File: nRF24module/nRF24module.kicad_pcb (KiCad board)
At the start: 2 copper layers, 40 x 20 mm, 31 parts, among them J1 SMA-RP, U1 nRF24L01P, U2 RFX2401C, X1 16MHz

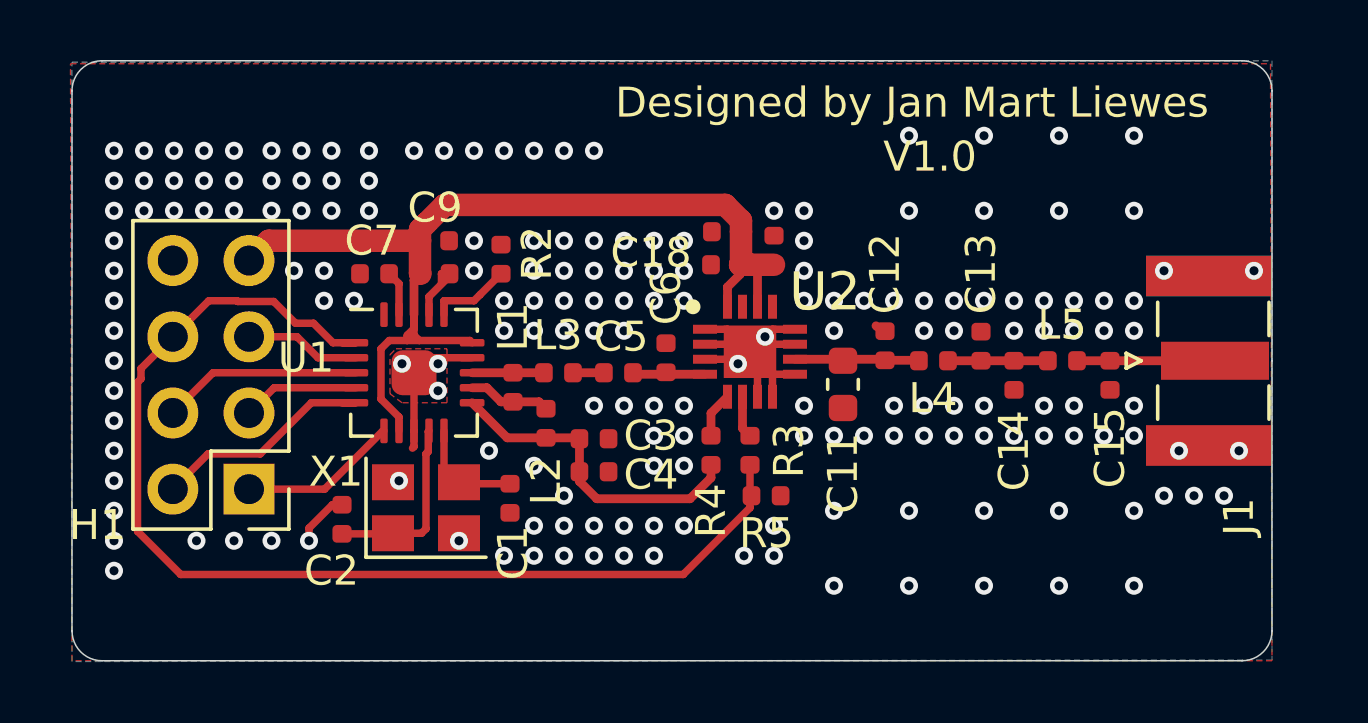
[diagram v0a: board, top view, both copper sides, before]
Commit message: Update, with Licence added to files, and rerouted PCB, cleaned up some things. Tightened up components, placed traces neater, placed vias neater. Added OSHW logo. TODO: Make own logo and add that.
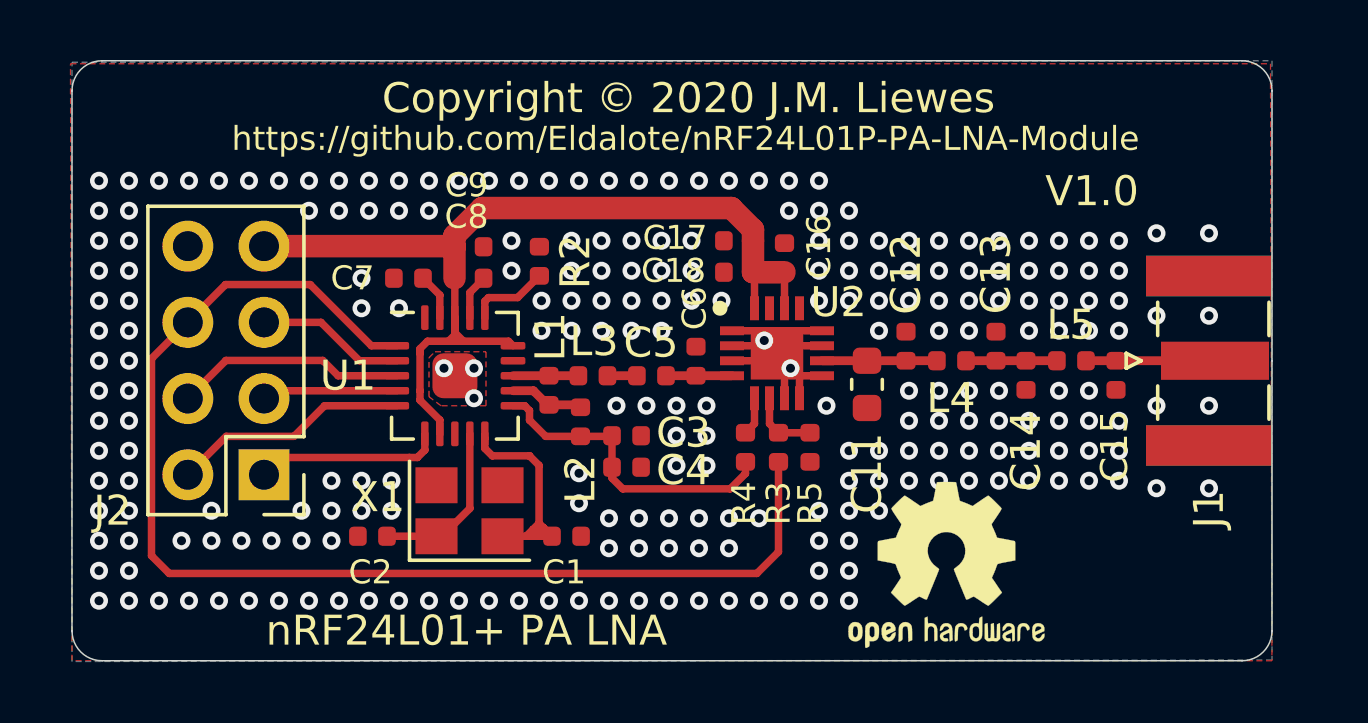
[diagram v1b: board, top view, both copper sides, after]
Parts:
- added LOGO1: Logo_Open_Hardware_Small, Symbol:OSHW-Logo2_7.3x6mm_SilkScreen, F.Cu at (148.8, 108.8)
- R5: value R_0402_1005Metric -> 2K
- moved C1 2.27 mm to (136.1, 107.8), turned to 180 degrees
- moved R5 2.18 mm to (144.2, 104.9), turned to 90 degrees
- moved X1 1.45 mm to (132.8, 107.0)
- moved U1 1.37 mm to (132.4, 102.5)
- moved R2 1.28 mm to (135.2, 98.7)
- moved L1 1.20 mm to (135.5, 103.0)
- moved C9 1.17 mm to (132.8, 98.2)
- moved C2 1.16 mm to (129.6, 107.8), turned to 0 degrees
- moved L3 1.15 mm to (137.0, 102.5)
- moved R4 1.15 mm to (142.1, 104.9)
- moved L2 1.15 mm to (136.6, 104.0)
- moved C8 1.14 mm to (132.8, 99.2)
- moved C7 1.14 mm to (130.8, 99.2)
- moved C5 1.10 mm to (138.9, 102.5)
- moved C4 1.10 mm to (138.1, 105.5)
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- renumbered H1 to J2
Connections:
- R5 pad 1: CE -> GND
- R5 pad 2: GND -> Net-(R3-Pad2)
- X1 pad 2: GND -> Net-(C1-Pad2)
- X1 pad 3: Net-(C1-Pad2) -> (no net)
- X1 pad 4: GND -> (no net)
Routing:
- net GND: track 21.4 -> 14.1 mm, vias 182 -> 242
- net Net-(C1-Pad2): track 3.64 -> 7.70 mm
- net CE: track 38.0 -> 41.1 mm
- net CSn: track 3.85 -> 4.96 mm
- net +3V3: track 33.9 -> 32.8 mm
- net SCLK: track 6.66 -> 7.70 mm
- net IRQ: track 5.30 -> 6.25 mm
- net Net-(R3-Pad2): track 1.40 -> 2.32 mm
- net MOSI: track 3.91 -> 4.53 mm
- net Net-(C2-Pad2): track 6.17 -> 5.63 mm
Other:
- net class 50Ohm  removed
- rule via_min_size: 0.4 -> 0.6
- board text added: "CE"
- board text added: "Copyright © 2020 J.M. Liewes"
- board text added: "IRQ"
- board text added: "MISO"
- board text added: "MOSI"
- board text added: "SCLK"
- board text added: "https://github.com/Eldalote/nRF24L01P-PA-LNA-Module"
- board text added: "nRF24L01+ PA LNA"
- board text added: "~CS"
- board text removed: "Designed by Jan Mart Liewes"

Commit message: Added licences, fixed crystal mistake
Signed-off-by: Eldalote <Eldalote.Electronics@gmail.com>
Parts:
- moved C1 1.72 mm to (135.9, 106.1)
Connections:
- X1 pad 2: Net-(C1-Pad2) -> GND
- X1 pad 3: (no net) -> Net-(C1-Pad2)
- X1 pad 4: (no net) -> GND
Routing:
- net Net-(C1-Pad2): track 7.70 -> 5.21 mm
- net GND: vias 242 -> 246
